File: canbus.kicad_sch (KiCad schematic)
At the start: 20 parts, among them J501 Conn_01x02, J601 Conn_01x04, U501 SN65HVD230DR, U502 ADuM1201AR, U603 MST5633BTE

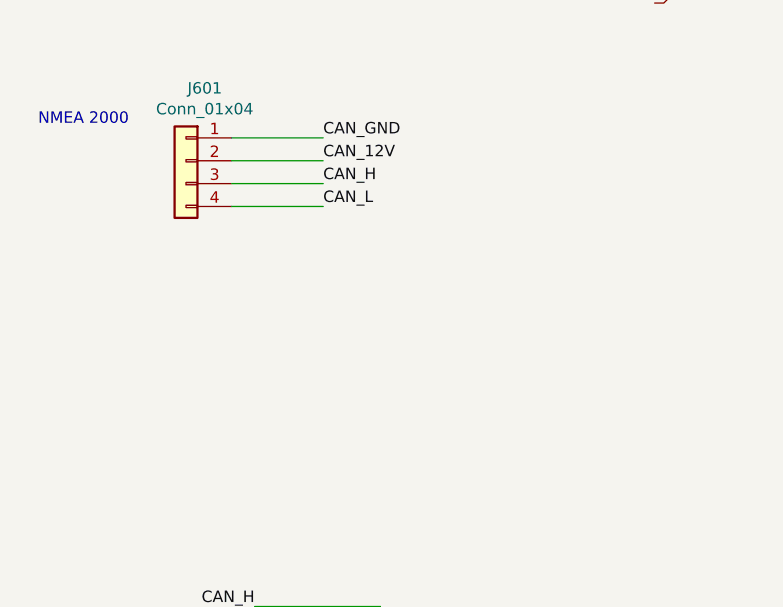
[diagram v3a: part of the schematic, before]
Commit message: Improve connector ESD protection; bump version to 2.0.2
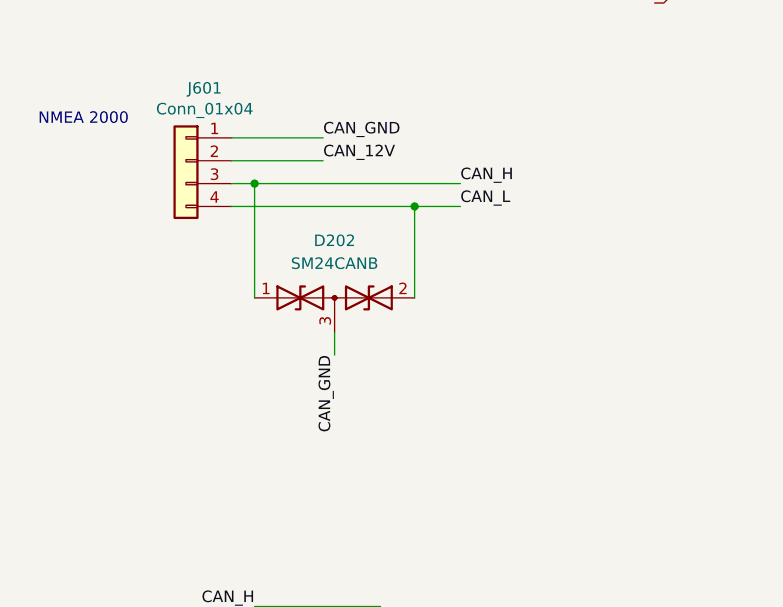
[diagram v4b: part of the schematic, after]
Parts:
- added D202: SM24CANB, Package_TO_SOT_SMD:SOT-23, symbol Device:D_TVS_Dual_AAC
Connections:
- net CAN_GND: now also D202.3 (common)
- net CAN_H: now also D202.1 (A1)
- net CAN_L: now also D202.2 (A2)
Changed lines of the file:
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@@
   (title_block
     (title "Sailor Hat with ESP32")
-    (date "2021-12-31")
-    (rev "2.0.1")
+    (date "2022-10-26")
+    (rev "2.0.2")
     (company "Hat Labs Ltd")
     (comment 1 "https://creativecommons.org/licenses/by-sa/4.0")
@@
   (junction (at 156.21 36.83) (diameter 0) (color 0 0 0 0)
   )
+  (junction (at 49.53 58.42) (diameter 0) (color 0 0 0 0)
+  )
   (junction (at 53.34 121.92) (diameter 0) (color 0 0 0 0)
   )
   (junction (at 194.31 36.83) (diameter 0) (color 0 0 0 0)
+  )
+  (junction (at 67.31 60.96) (diameter 0) (color 0 0 0 0)
   )
   (junction (at 162.56 36.83) (diameter 0) (color 0 0 0 0)
@@
     (stroke (width 0) (type default) (color 0 0 0 0))
   )
-  (wire (pts (xy 46.99 60.96) (xy 57.15 60.96))
+  (wire (pts (xy 46.99 60.96) (xy 67.31 60.96))
     (stroke (width 0) (type default) (color 0 0 0 0))
   )
@@
     (stroke (width 0) (type default) (color 0 0 0 0))
   )
-  (wire (pts (xy 46.99 58.42) (xy 57.15 58.42))
-    (stroke (width 0) (type default) (color 0 0 0 0))
-  )
   (wire (pts (xy 161.29 107.95) (xy 144.78 107.95))
     (stroke (width 0) (type default) (color 0 0 0 0))
@@
     (stroke (width 0) (type default) (color 0 0 0 0))
   )
+  (wire (pts (xy 58.42 74.93) (xy 58.42 77.47))
+    (stroke (width 0) (type default) (color 0 0 0 0))
+  )
+  (wire (pts (xy 49.53 71.12) (xy 49.53 58.42))
+    (stroke (width 0) (type default) (color 0 0 0 0))
+  )
   (wire (pts (xy 121.92 88.9) (xy 128.27 88.9))
     (stroke (width 0) (type default) (color 0 0 0 0))
@@
     (stroke (width 0) (type default) (color 0 0 0 0))
   )
+  (wire (pts (xy 67.31 60.96) (xy 72.39 60.96))
+    (stroke (width 0) (type default) (color 0 0 0 0))
+  )
+  (wire (pts (xy 49.53 58.42) (xy 72.39 58.42))
+    (stroke (width 0) (type default) (color 0 0 0 0))
+  )
   (wire (pts (xy 165.1 119.38) (xy 166.37 119.38))
     (stroke (width 0) (type default) (color 0 0 0 0))
@@
     (stroke (width 0) (type default) (color 0 0 0 0))
   )
+  (wire (pts (xy 46.99 58.42) (xy 49.53 58.42))
+    (stroke (width 0) (type default) (color 0 0 0 0))
+  )
   (wire (pts (xy 162.56 36.83) (xy 170.18 36.83))
     (stroke (width 0) (type default) (color 0 0 0 0))
@@
   )
   (wire (pts (xy 165.1 106.68) (xy 166.37 106.68))
+    (stroke (width 0) (type default) (color 0 0 0 0))
+  )
+  (wire (pts (xy 67.31 60.96) (xy 67.31 71.12))
     (stroke (width 0) (type default) (color 0 0 0 0))
   )
@@
     (effects (font (size 1.27 1.27)) (justify right bottom))
   )
-  (label "CAN_H" (at 57.15 58.42 0)
+  (label "CAN_H" (at 72.39 58.42 0)
     (effects (font (size 1.27 1.27)) (justify left bottom))
   )
@@
     (effects (font (size 1.27 1.27)) (justify right bottom))
   )
+  (label "CAN_GND" (at 58.42 77.47 270)
+    (effects (font (size 1.27 1.27)) (justify right bottom))
+  )
   (label "CAN_H" (at 49.53 105.41 180)
     (effects (font (size 1.27 1.27)) (justify right bottom))
@@
     (effects (font (size 1.27 1.27)) (justify right bottom))
   )
-  (label "CAN_L" (at 57.15 60.96 0)
+  (label "CAN_L" (at 72.39 60.96 0)
     (effects (font (size 1.27 1.27)) (justify left bottom))
   )
@@
     (pin "2")
   )
+  (symbol (lib_id "Device:D_TVS_Dual_AAC") (at 58.42 71.12 0) (unit 1)
+    (in_bom yes) (on_board yes) (fields_autoplaced)
+    (property "Reference" "D202" (id 0) (at 58.42 64.77 0))
+    (property "Value" "SM24CANB" (id 1) (at 58.42 67.31 0))
+    (property "Footprint" "Package_TO_SOT_SMD:SOT-23" (id 2) (at 54.61 71.12 0)
+      (effects (font (size 1.27 1.27)) hide)
+    )
+    (property "Datasheet" "~" (id 3) (at 54.61 71.12 0)
+      (effects (font (size 1.27 1.27)) hide)
+    )
+    (property "LCSC" "C970029" (id 4) (at 58.42 71.12 0)
+      (effects (font (size 1.27 1.27)) hide)
+    )
+    (pin "1")
+    (pin "2")
+    (pin "3")
+  )
   (symbol (lib_id "power:+3.3V") (at 219.71 97.79 0) (unit 1)

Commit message: Save schema with KiCad 7.0.6
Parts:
- D202, U501, U502, U603: JLCPCB_CORRECTION (none) -> 0;0;180

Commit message: Fix component rotations
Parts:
- J601: JLCPCB_CORRECTION (none) -> 5.715;0;180
- U501, U502: JLCPCB_CORRECTION 0;0;180 -> 0;0;270
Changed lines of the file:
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@@
       (effects (font (size 1.27 1.27)) hide)
     )
-    (property "JLCPCB_CORRECTION" "" (at 41.91 55.88 0)
+    (property "JLCPCB_CORRECTION" "5.715;0;180" (at 41.91 55.88 0)
       (effects (font (size 1.27 1.27)) hide)
     )
@@
       (effects (font (size 1.27 1.27)) hide)
     )
-    (property "JLCPCB_CORRECTION" "0;0;180" (at 179.07 111.76 0)
+    (property "JLCPCB_CORRECTION" "0;0;270" (at 179.07 111.76 0)
       (effects (font (size 1.27 1.27)) hide)
     )
@@
       (effects (font (size 1.27 1.27)) hide)
     )
-    (property "JLCPCB_CORRECTION" "0;0;180" (at 134.62 110.49 0)
-      (effects (font (size 1.27 1.27)) hide)
-    )
+    (property "JLCPCB_CORRECTION" "0;0;270" (at 134.62 110.49 0)
+      (effects (font (size 1.27 1.27)) hide)
+    )

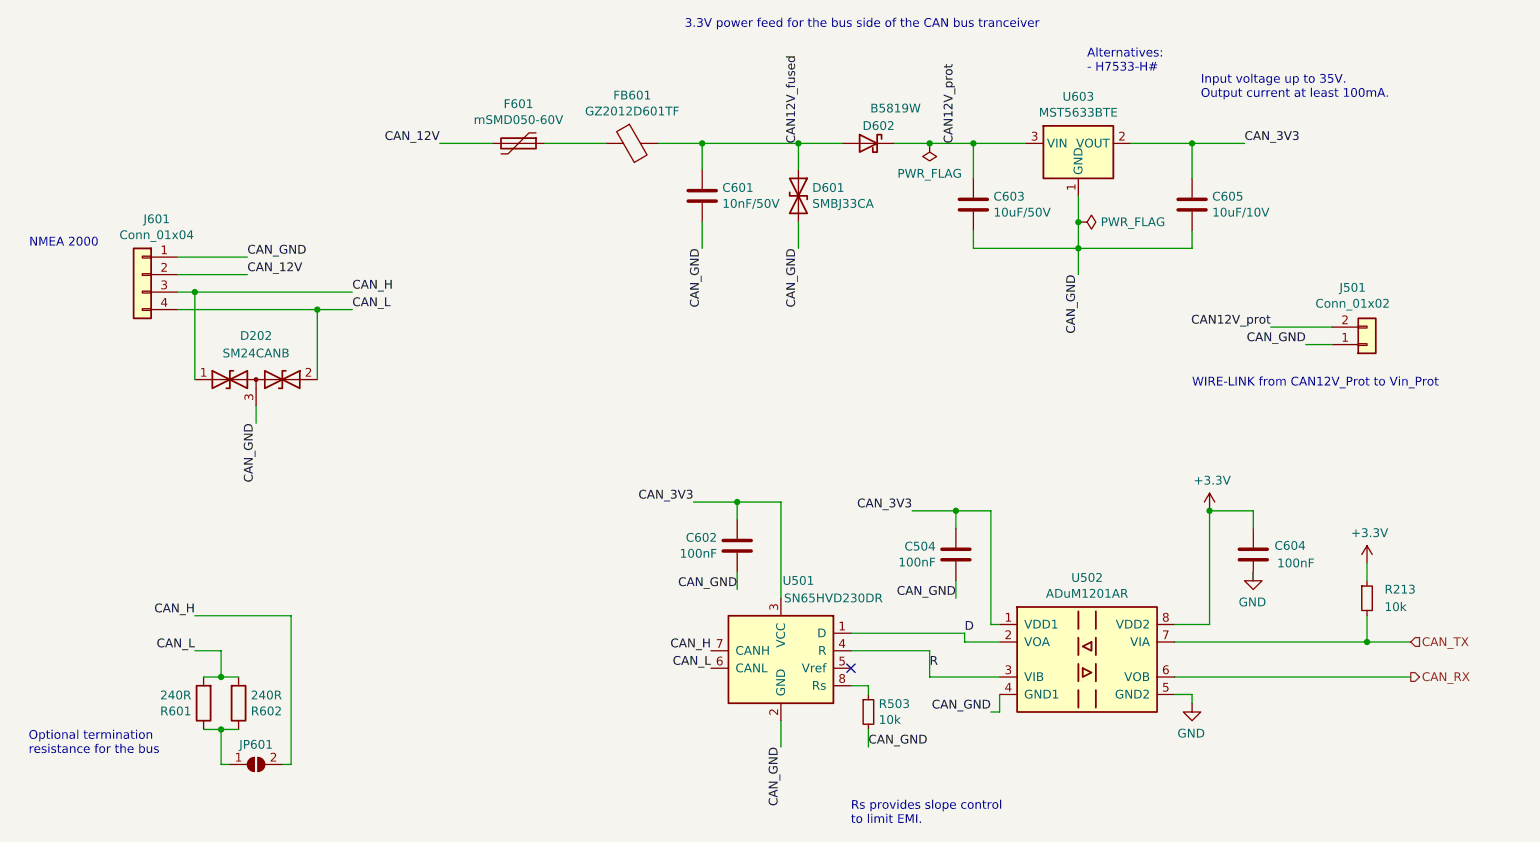
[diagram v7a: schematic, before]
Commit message: Go back to ISO1050 for CAN transceiver
Also add CAN RX and TX LEDs and beef up buck capacitors
as much as space allows.
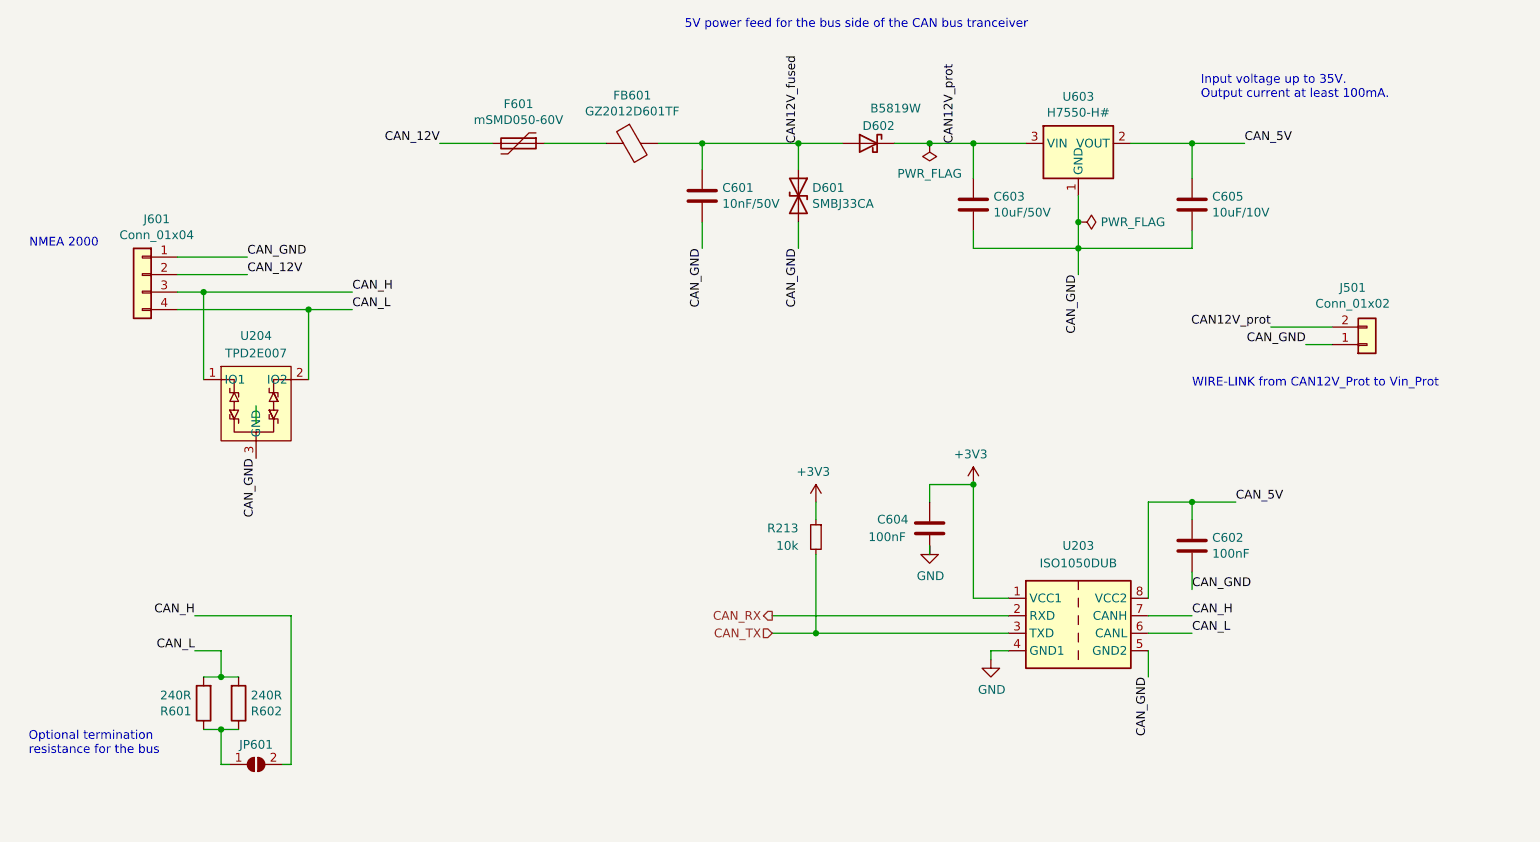
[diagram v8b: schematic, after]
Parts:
- removed C504: 100nF, Capacitor_SMD:C_0402_1005Metric, symbol Device:C
- removed D202: SM24CANB, Package_TO_SOT_SMD:SOT-23, symbol Device:D_TVS_Dual_AAC
- removed R503: 10k, Resistor_SMD:R_0402_1005Metric, symbol Device:R_Small
- removed U501: SN65HVD230DR, Package_SO:SOIC-8_3.9x4.9mm_P1.27mm, symbol Interface_CAN_LIN:SN65HVD231
- removed U502: ADuM1201AR, Package_SO:SOIC-8_3.9x4.9mm_P1.27mm, symbol Isolator:ADuM1201AR
- added U203: ISO1050DUB, Package_SO:SOP-8_6.62x9.15mm_P2.54mm, symbol Interface_CAN_LIN:ISO1050DUB
- added U204: TPD2E007, Package_TO_SOT_SMD:SOT-323_SC-70, symbol SH-ESP32:TPD2E007
- U603: value MST5633BTE -> H7550-H#; LCSC C525415 -> C277875
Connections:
- net +3V3: now also U203.1 (VCC1)
- net CAN_GND: now also U203.5 (GND2), U204.3 (GND)
- net CAN_H: now also U203.7 (CANH), U204.1 (IO1)
- net CAN_L: now also U203.6 (CANL), U204.2 (IO2)
- net CAN_RX: now also U203.2 (RXD)
- net CAN_TX: now also U203.3 (TXD)
- net GND: now also U203.4 (GND1)
- net CAN_3V3 renamed CAN_5V
- net CAN_5V: now also U203.8 (VCC2)
- no-connect marks 1 -> 0
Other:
- note added: "5V power feed for the bus side of the CAN bus tranceiver"
- note removed: "3.3V power feed for the bus side of the CAN bus tranceiver"
- note removed: "Alternatives: - H7533-H#"
- note removed: "Rs provides slope control to limit EMI."
- company: Hat Labs Ltd -> Hat Labs Oy
- title: Sailor Hat with ESP32 -> SH-ESP32
- moved on the sheet: C602, C604, R213
